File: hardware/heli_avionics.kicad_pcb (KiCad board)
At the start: 4 copper layers, 65.5 x 39 mm, 72 parts, among them J1 Pin_Header_2x3, J2 JST_PH_01x02, J3 JST_XH_01x02, J4 JST_XH_01x02, J5 JST_PH_01x03, J6 Conn_01x01, J7 JST_ZH_01x02, J8 Conn_01x01, Q1 AO3400A, SW1 Reset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

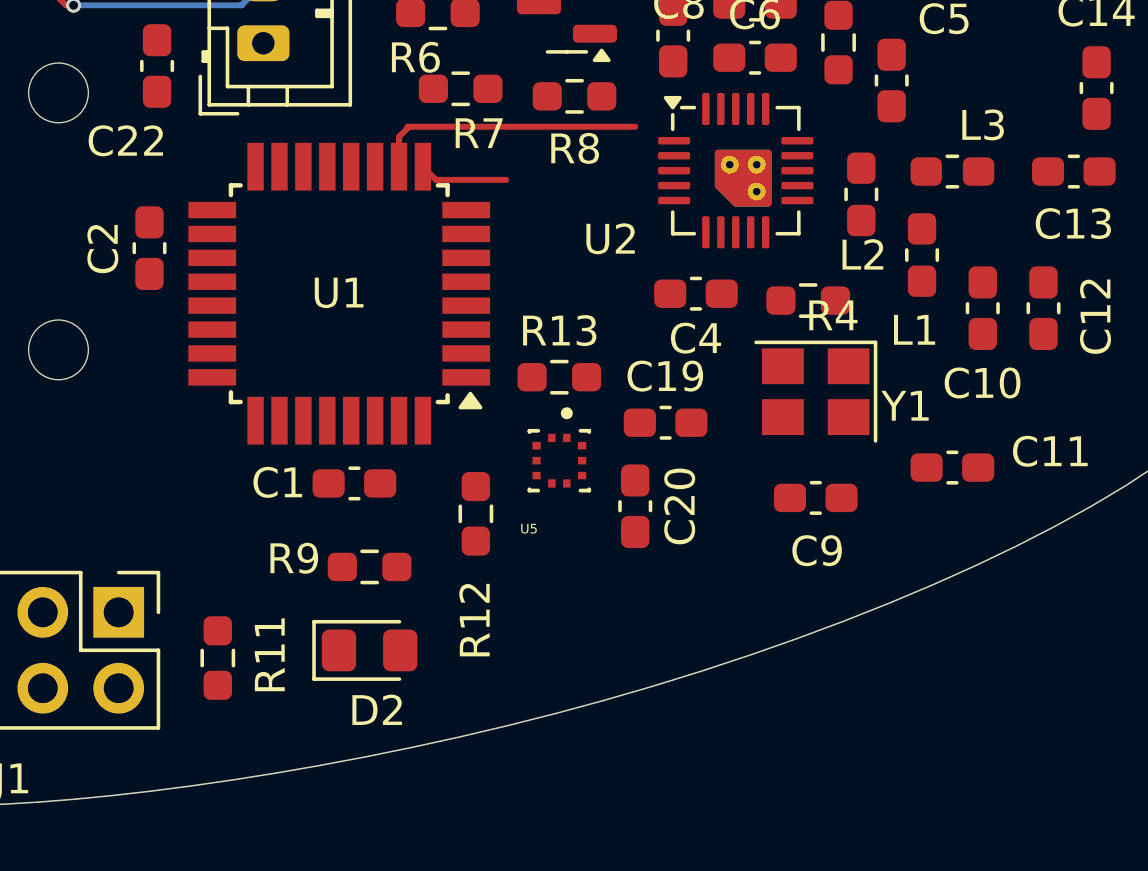
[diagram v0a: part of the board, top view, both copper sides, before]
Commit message: Added pin headers for external connections (PA6 and I2C)
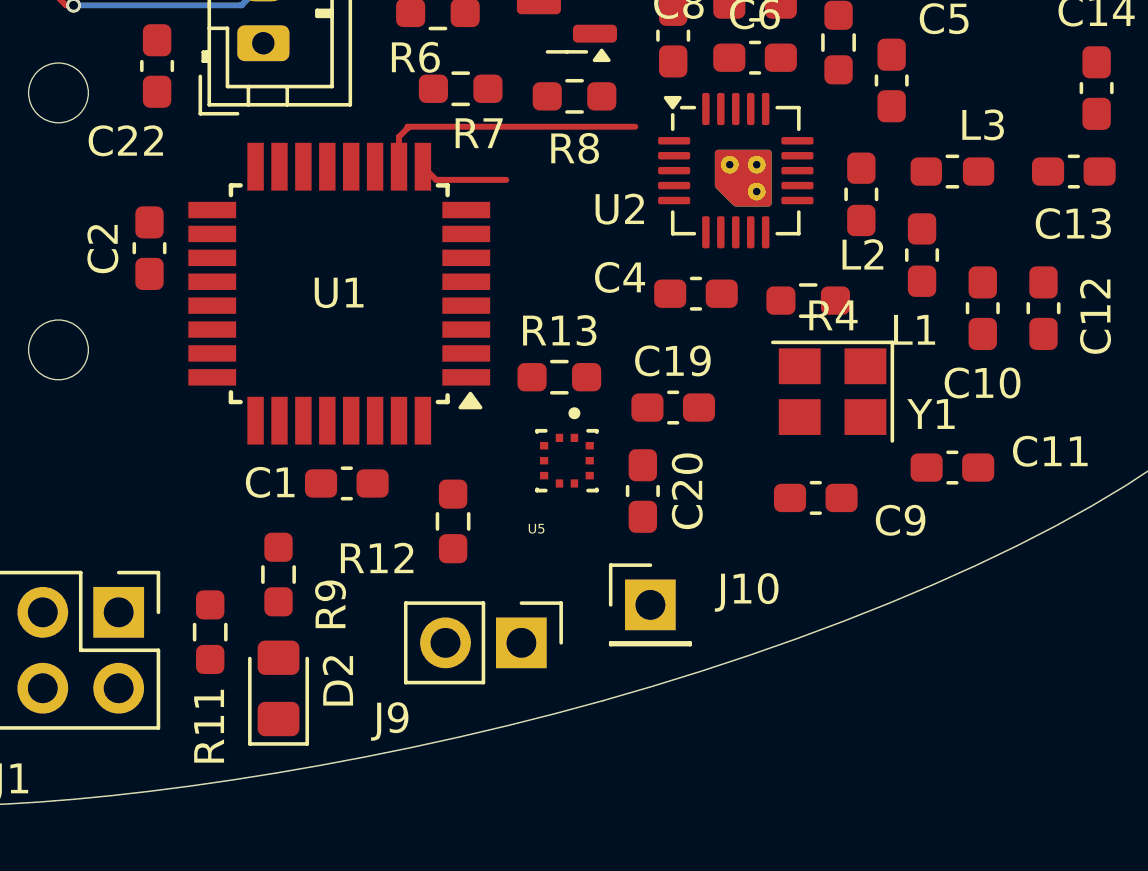
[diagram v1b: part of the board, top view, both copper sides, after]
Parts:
- added J10: Pin_Header_1x1, Connector_PinHeader_2.54mm:PinHeader_1x01_P2.54mm_Vertical, F.Cu at (143.5, 132.3)
- added J9: Pin_Header_1x2, Connector_PinHeader_2.54mm:PinHeader_1x02_P2.54mm_Vertical, F.Cu at (139.2, 133.6)
- moved D2 3.30 mm to (131.1, 135.1), turned to 90 degrees
- moved R9 3.06 mm to (131.1, 131.3), turned to 90 degrees
- moved R11 0.90 mm to (128.8, 133.2)
- moved R12 0.80 mm to (136.9, 129.5)
- moved C20 0.57 mm to (143.3, 128.5)
- moved C19 0.57 mm to (144.3, 125.7)
- moved Y1 0.56 mm to (149.6, 125.2)
- moved C1 0.25 mm to (133.3, 128.3)
- moved U5 0.25 mm to (140.7, 127.5)
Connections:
- U1 pad 3: unconnected-(U1-PA5-Pad3) -> Net-(J10-Pin_1)

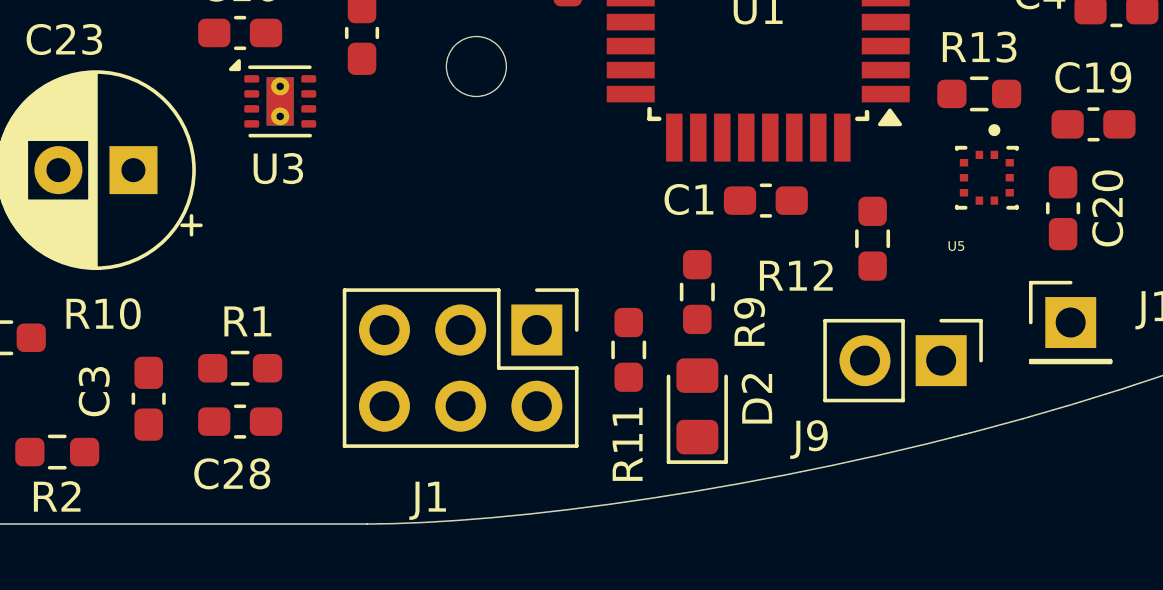
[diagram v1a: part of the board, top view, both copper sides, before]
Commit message: Reordered pins on programming connector for cleaner routing
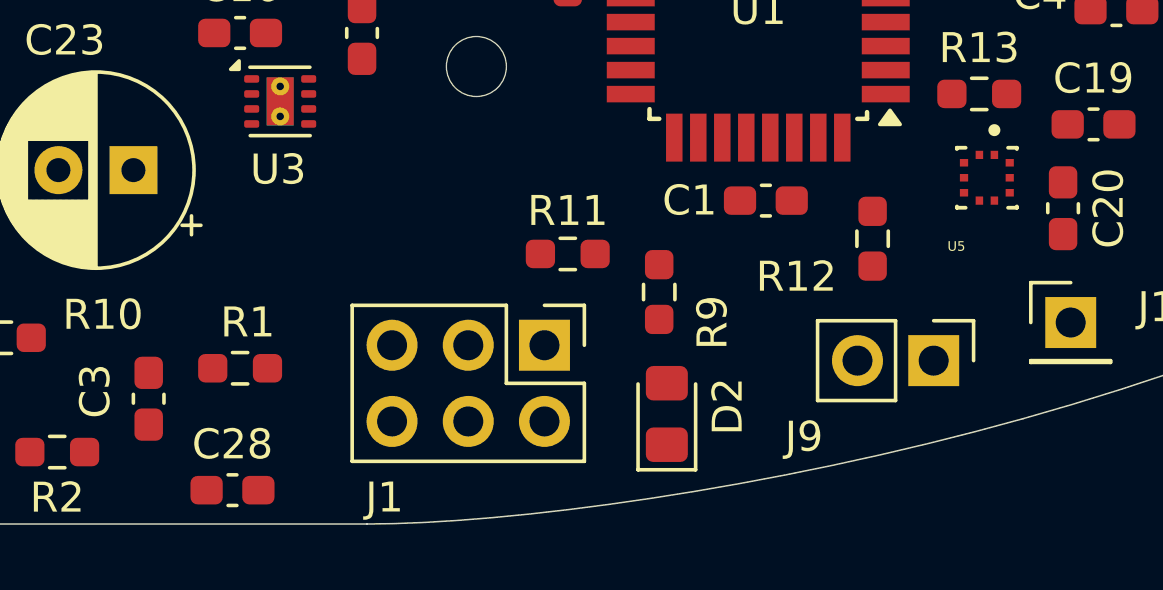
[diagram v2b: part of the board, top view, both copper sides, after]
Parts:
- moved R11 3.79 mm to (126.7, 130.0), turned to 0 degrees
- moved C28 2.30 mm to (115.6, 137.9)
- moved R9 1.27 mm to (129.8, 131.3)
- moved D2 1.05 mm to (130.0, 135.4)
- moved J1 0.57 mm to (126.0, 133.1)
- moved J9 0.25 mm to (138.9, 133.6)
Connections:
- C28 pad 2: Net-(J1-Pin_6) -> Net-(J1-Pin_4)
- J1 pad 1: VCC -> /PA0
- J1 pad 2: GND -> /PA1
- J1 pad 3: /PA0 -> Net-(J1-Pin_3)
- J1 pad 5: /PA1 -> VCC
- J1 pad 6: Net-(J1-Pin_6) -> GND
- R11 pad 1: Net-(J1-Pin_4) -> Net-(J1-Pin_3)

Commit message: Shifted some things around
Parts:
- moved TP1 11.0 mm to (133.3, 104.4)
- moved TP4 8.92 mm to (142.5, 100.1)
- moved C21 5.36 mm to (126.2, 109.2)
- moved U6 2.03 mm to (122.9, 109.7), turned to -90 degrees
- moved C23 1.20 mm to (113.2, 128.0)
- moved C16 1.05 mm to (116.8, 122.4)
- moved J6 0.57 mm to (122.4, 104.1)
- moved R1 0.57 mm to (116.3, 133.6)
- moved C3 0.51 mm to (112.8, 135.4)
- moved U7 0.51 mm to (141.4, 108.0)
- moved J2 0.51 mm to (103.1, 124.4)
- moved R13 0.36 mm to (140.7, 124.5)
- moved C17 0.36 mm to (116.6, 114.6)
- moved R7 0.36 mm to (136.9, 115.3)
- moved R10 0.36 mm to (108.2, 133.1)
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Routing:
- net /Power circuits/VREG_EN: track 13.4 -> 0.00 mm, vias 1 -> 0
- net /PD0: track 9.08 -> 0.00 mm
- net /SPI_SS: track 2.97 -> 0.00 mm
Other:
- board text added: "+"
- board text added: "-"
- board text added: "3V"
- board text added: "GPIO PA6"
- board text added: "Reset"
- board text added: "SCL"
- board text added: "SDA"

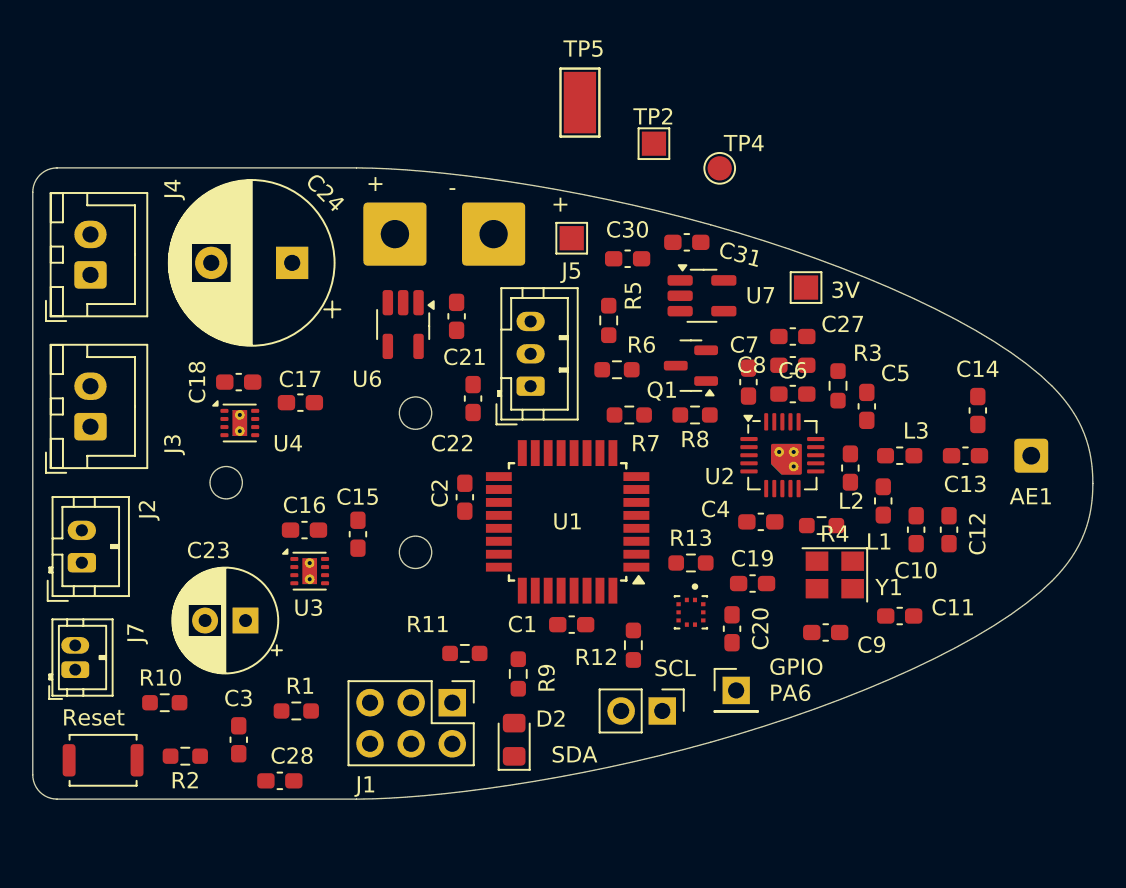
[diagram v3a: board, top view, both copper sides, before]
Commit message: Shifted radio components and testpoints around
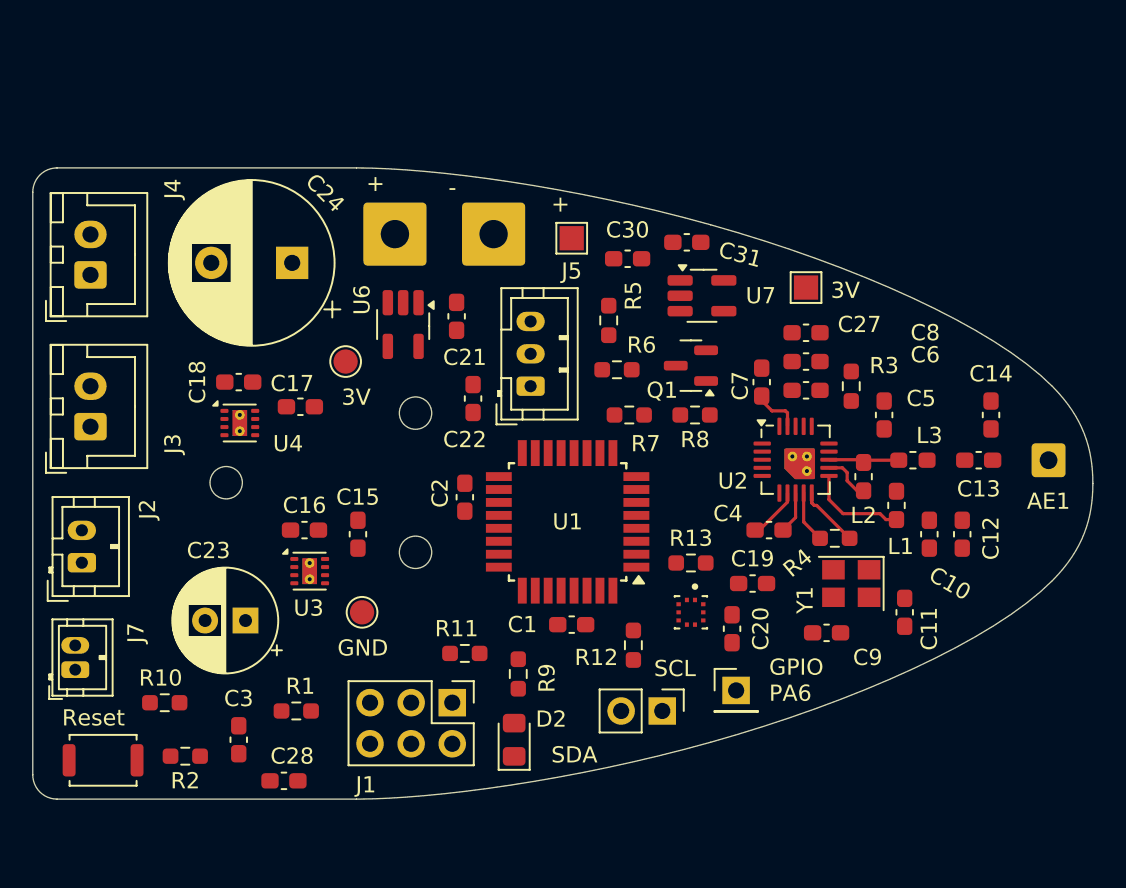
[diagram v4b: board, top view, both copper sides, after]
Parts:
- removed TP5: TestPoint, TestPoint:TestPoint_Keystone_5019_Minature
- TP2: footprint TestPoint:TestPoint_Pad_1.5x1.5mm -> TestPoint:TestPoint_Pad_D1.5mm
- moved TP4 35.2 mm to (120.4, 127.5)
- moved TP2 23.3 mm to (119.4, 112.0)
- moved C5 1.20 mm to (152.7, 115.3)
- moved Y1 1.15 mm to (150.6, 125.7)
- moved R4 1.13 mm to (149.6, 122.9)
- moved AE1 1.11 mm to (162.8, 118.1)
- moved L2 0.97 mm to (151.4, 119.1)
- moved C10 0.86 mm to (155.4, 122.7)
- moved C13 0.86 mm to (158.5, 118.1)
- moved C14 0.86 mm to (159.3, 115.3)
- moved C12 0.86 mm to (157.5, 122.7)
- moved L1 0.86 mm to (153.4, 120.9)
- moved L3 0.86 mm to (154.4, 118.1)
- moved U2 0.86 mm to (147.2, 118.1)
- moved C8 0.85 mm to (147.8, 112.0)
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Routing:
- net Net-(U2-VDD_PA): track 0.00 -> 6.15 mm
- net Net-(U2-ANT2): track 0.00 -> 4.44 mm
- net Net-(U2-XC1): track 0.00 -> 3.85 mm
- net +3V0: track 0.00 -> 3.27 mm
- net Net-(U2-XC2): track 0.00 -> 3.21 mm
- net Net-(U2-ANT1): track 0.00 -> 3.03 mm
- net Net-(U2-DVDD): track 0.00 -> 2.74 mm
- net GND: track 0.00 -> 2.61 mm
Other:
- board text added: "GND"

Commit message: Routed most of the radio traces
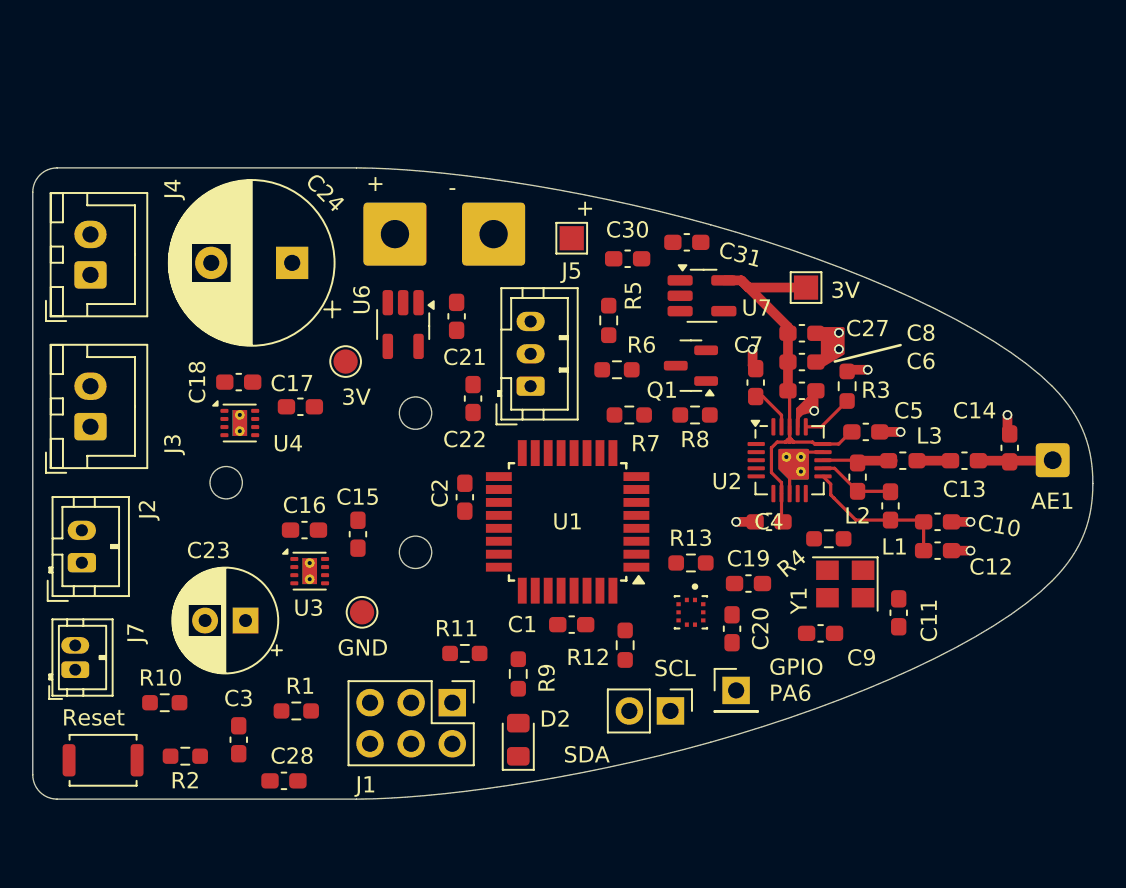
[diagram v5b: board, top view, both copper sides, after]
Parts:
- moved C14 2.34 mm to (160.4, 117.3)
- moved C12 1.83 mm to (156.0, 123.7), turned to 0 degrees
- moved C5 1.54 mm to (151.5, 116.4), turned to 0 degrees
- moved C10 0.92 mm to (156.0, 121.9), turned to 0 degrees
- moved C13 0.88 mm to (157.6, 118.1)
- moved L3 0.63 mm to (153.8, 118.1)
- moved R12 0.51 mm to (136.7, 129.5)
- moved C4 0.51 mm to (145.5, 121.9), turned to 180 degrees
- moved J9 0.51 mm to (139.5, 133.6)
- moved C9 0.37 mm to (148.7, 128.8)
- moved C7 0.37 mm to (144.7, 113.3)
- moved Y1 0.37 mm to (150.3, 125.8)
- moved C11 0.37 mm to (153.6, 127.5)
- moved L1 0.37 mm to (153.0, 120.9)
- moved U2 0.37 mm to (146.8, 118.1)
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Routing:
- net +3V0: track 3.27 -> 28.9 mm
- net GND: track 2.61 -> 17.9 mm, vias 0 -> 10
- net Net-(AE1-A): track 0.00 -> 4.84 mm
- net Net-(U2-XC1): track 3.85 -> 0.00 mm
- net Net-(U2-VDD_PA): track 6.15 -> 9.65 mm
- net Net-(U2-IREF): track 0.00 -> 3.22 mm
- net Net-(U2-XC2): track 3.21 -> 0.00 mm
- net Net-(C13-Pad1): track 0.00 -> 2.07 mm
- net Net-(U2-ANT1): track 3.03 -> 4.77 mm
